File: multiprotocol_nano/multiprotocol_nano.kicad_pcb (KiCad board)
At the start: 2 copper layers, 32 x 55.6 mm, 7 parts, among them J1 Conn_01x05, J3 Conn_01x03, U1 NRF24L01_Breakout

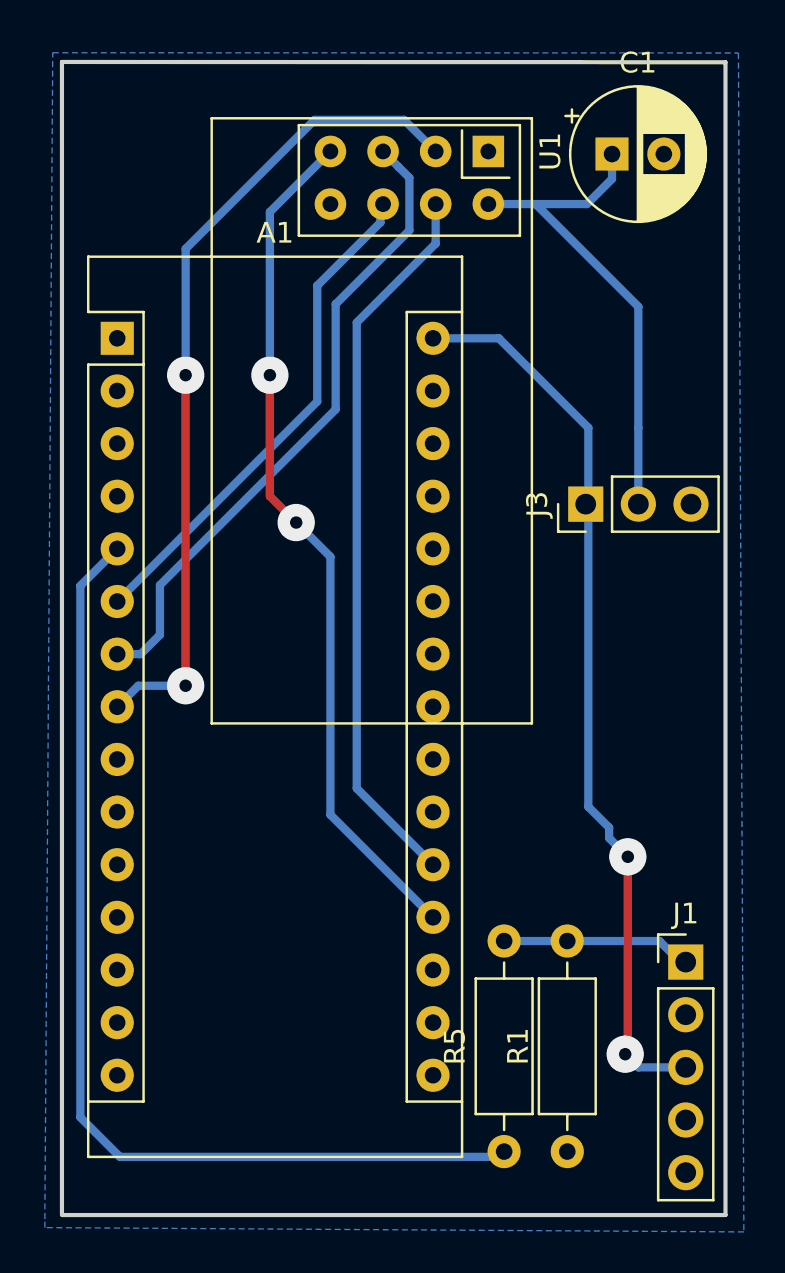
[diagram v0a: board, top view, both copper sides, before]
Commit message: Fix wrong package for LM317
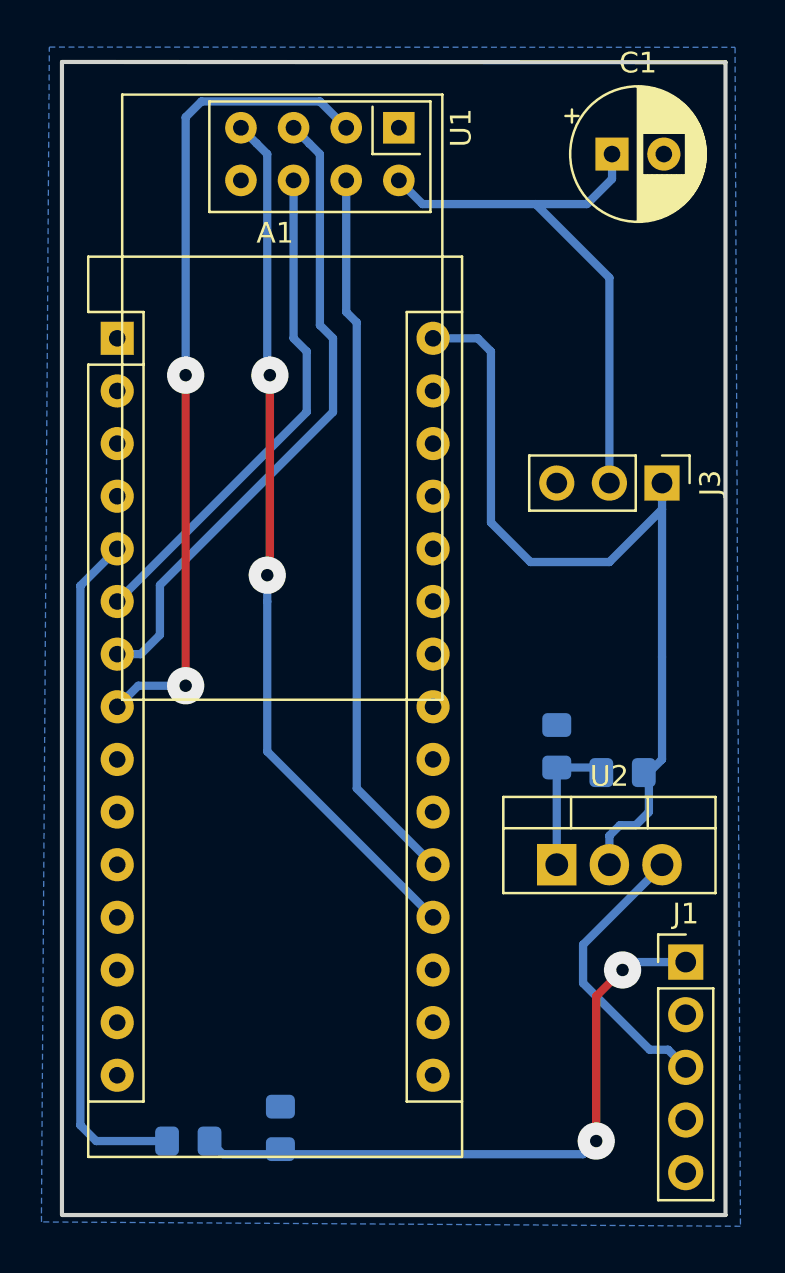
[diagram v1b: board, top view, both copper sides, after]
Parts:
- added R2: 1.2K, Resistor_SMD:R_0805_2012Metric_Pad1.15x1.40mm_HandSolder, B.Cu at (181.6, 108.6)
- added R3: 240, Resistor_SMD:R_0805_2012Metric_Pad1.15x1.40mm_HandSolder, B.Cu at (184.8, 109.9)
- added U2: LM317_3PinPackage, Package_TO_SOT_THT:TO-220-3_Vertical, F.Cu at (181.6, 114.3)
- R1, R5: footprint Resistor_THT:R_Axial_DIN0207_L6.3mm_D2.5mm_P10.16mm_Horizontal -> Resistor_SMD:R_0805_2012Metric_Pad1.15x1.40mm_HandSolder; moved to B.Cu
- moved R5 15.2 mm to (163.8, 127.6), turned to 0 degrees
- moved R1 13.9 mm to (168.3, 127.0), turned to 270 degrees
- moved U1 4.47 mm to (174.0, 78.7)
- moved J3 3.82 mm to (186.7, 95.9), turned to 270 degrees
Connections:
- A1 pad 30: +BATT -> VCC
- J3 pad 1: +BATT -> VCC
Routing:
- net VCC: track 0.00 -> 41.6 mm
- net +BATT: track 43.7 -> 13.9 mm, vias 2 -> 0
- net PPM: track 9.18 -> 31.4 mm, vias 0 -> 2
- net PPM_IN: track 49.5 -> 33.0 mm
- net Net-(R2-Pad2): track 0.00 -> 7.29 mm
- net +3V3: track 24.2 -> 27.4 mm
- net MISO: track 41.4 -> 42.0 mm
